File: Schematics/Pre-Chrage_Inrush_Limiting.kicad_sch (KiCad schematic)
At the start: 6 parts, among them J7 464379202, J8 464369202, Q1 STB10NK60ZT4

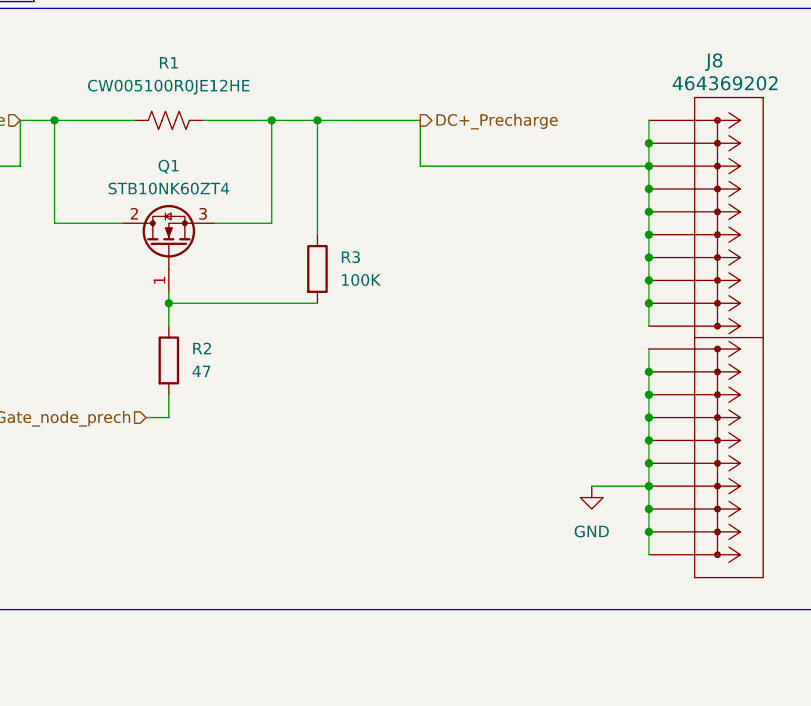
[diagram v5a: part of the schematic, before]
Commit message: [Milestone Compelted Controller and USB]
- Added Test Points
- Completed USB circuit to Controller
- Wired up Controller
- Added Connectors to Power Subsheet and 12pin from cotnroller to Full
  Bridge
- Added 3d models for USB compoents
- General fixes to subsheets
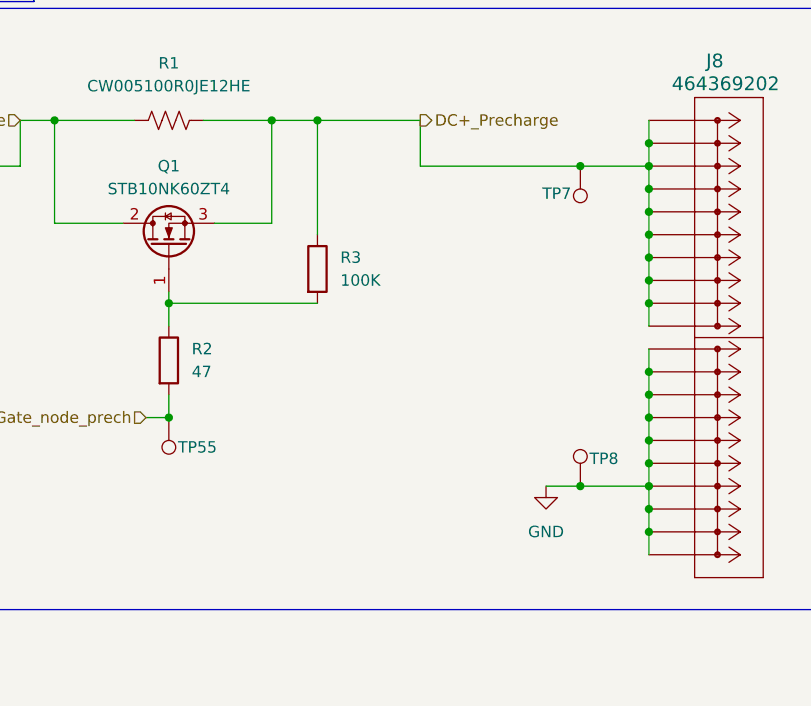
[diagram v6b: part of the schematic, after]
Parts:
- added TP55, TP7: 5277, SiC_Inverter:5277, symbol SiC_Inverter:5277
- added TP8: 5281, SiC_Inverter:5281, symbol SiC_Inverter:5281
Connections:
- net DC+_Precharge: now also TP7.1
- net GND: now also TP8.1
- net Gate_node_prech: now also TP55.1

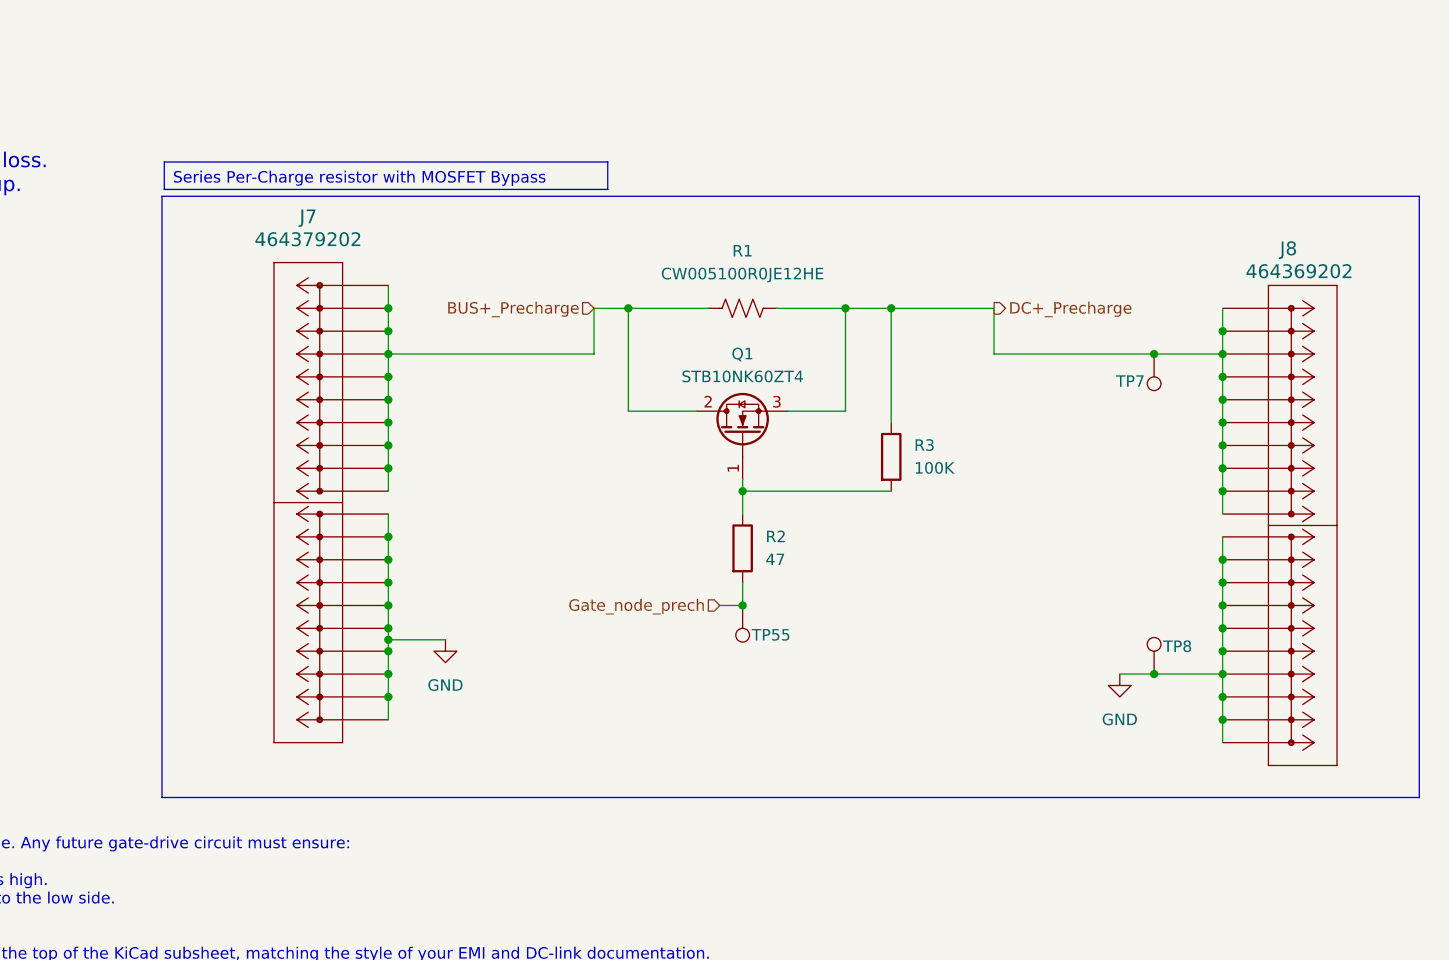
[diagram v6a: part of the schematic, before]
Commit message: [WIP Input Protection Circuit to Controller]
- Added Gate node input protection pin to controller
- Added optocoupler to input protection circuit
- Added 3d model for PC817.....
- Updated PCB to test out PCB modularity
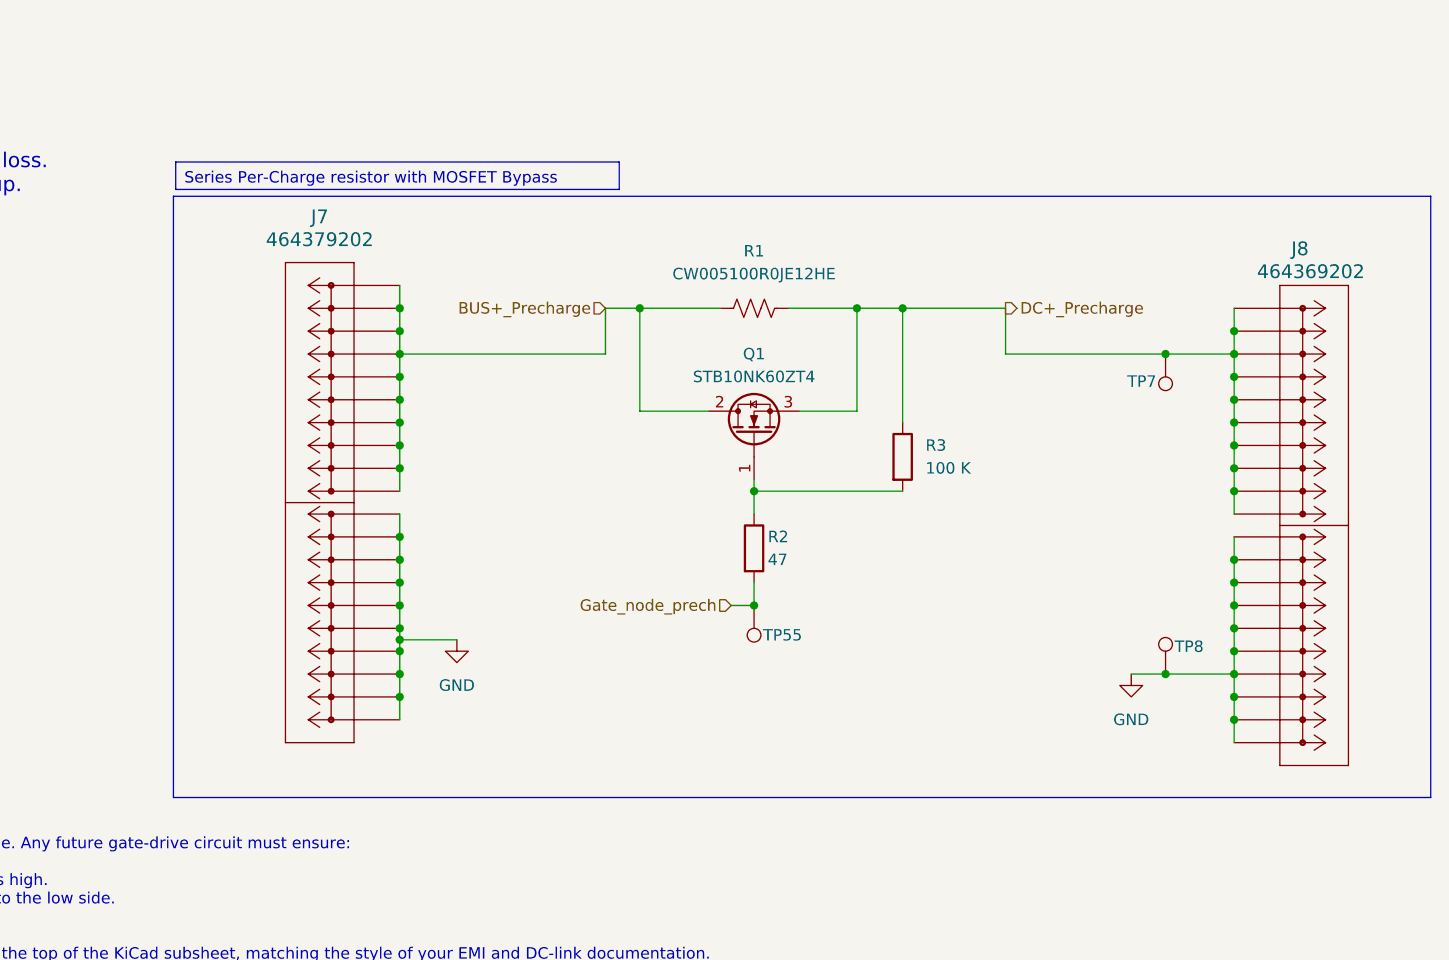
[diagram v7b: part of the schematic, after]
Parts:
- R2: symbol Device:R -> SiC_Inverter:RT1206FRE0747RL
- R3: value 100K -> 100 K; symbol Device:R -> SiC_Inverter:RT1206BRD07100KL
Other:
- moved on the sheet: J7, J8, Q1, R1, R2, R3, TP55, TP7, TP8

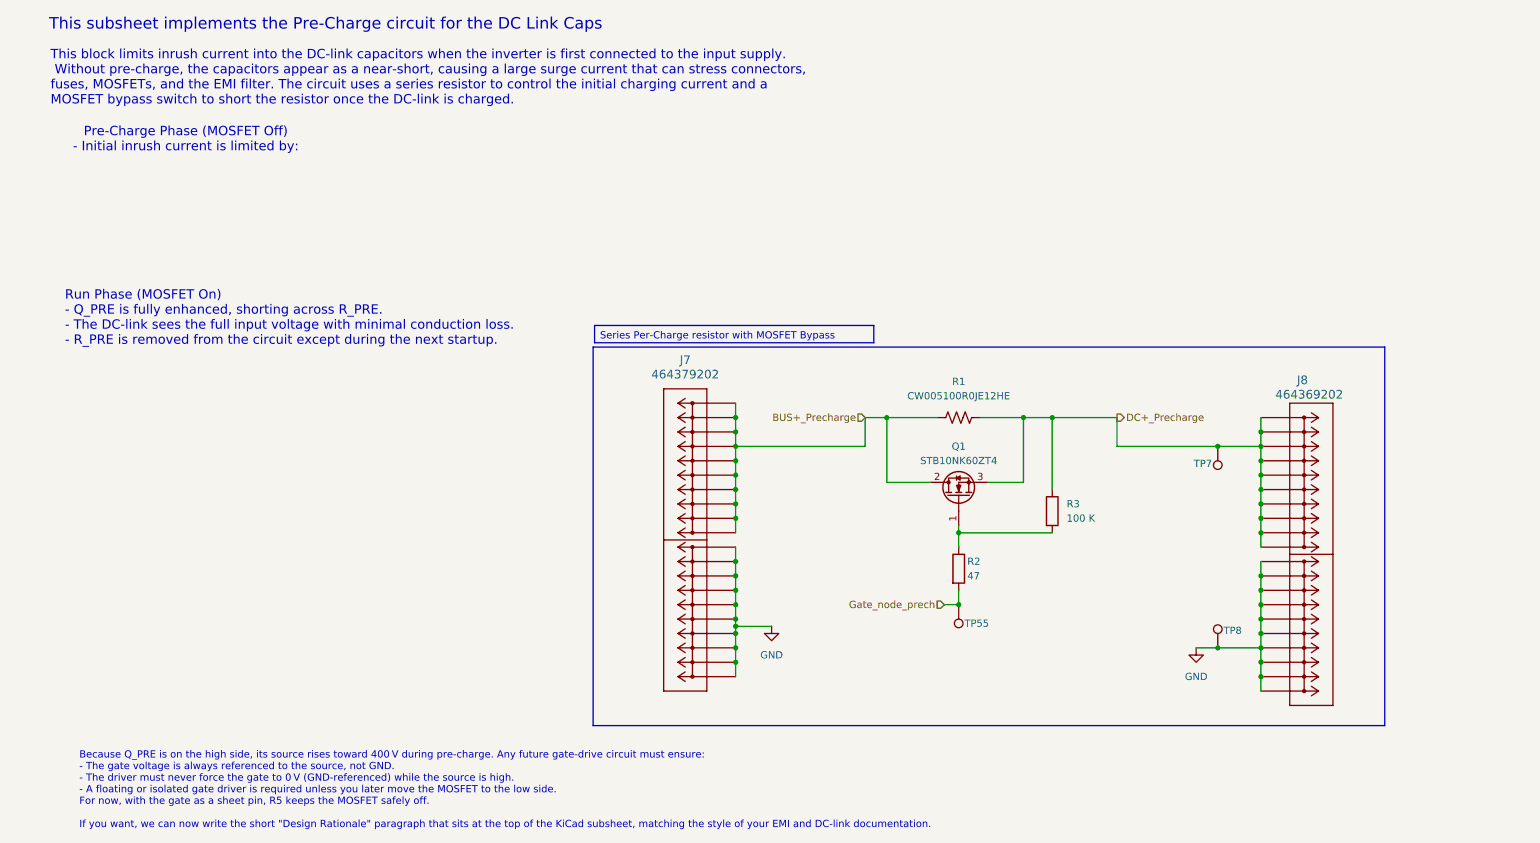
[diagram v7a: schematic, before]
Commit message: Added Precharge Gate Driver to controller and per charge sub circuit
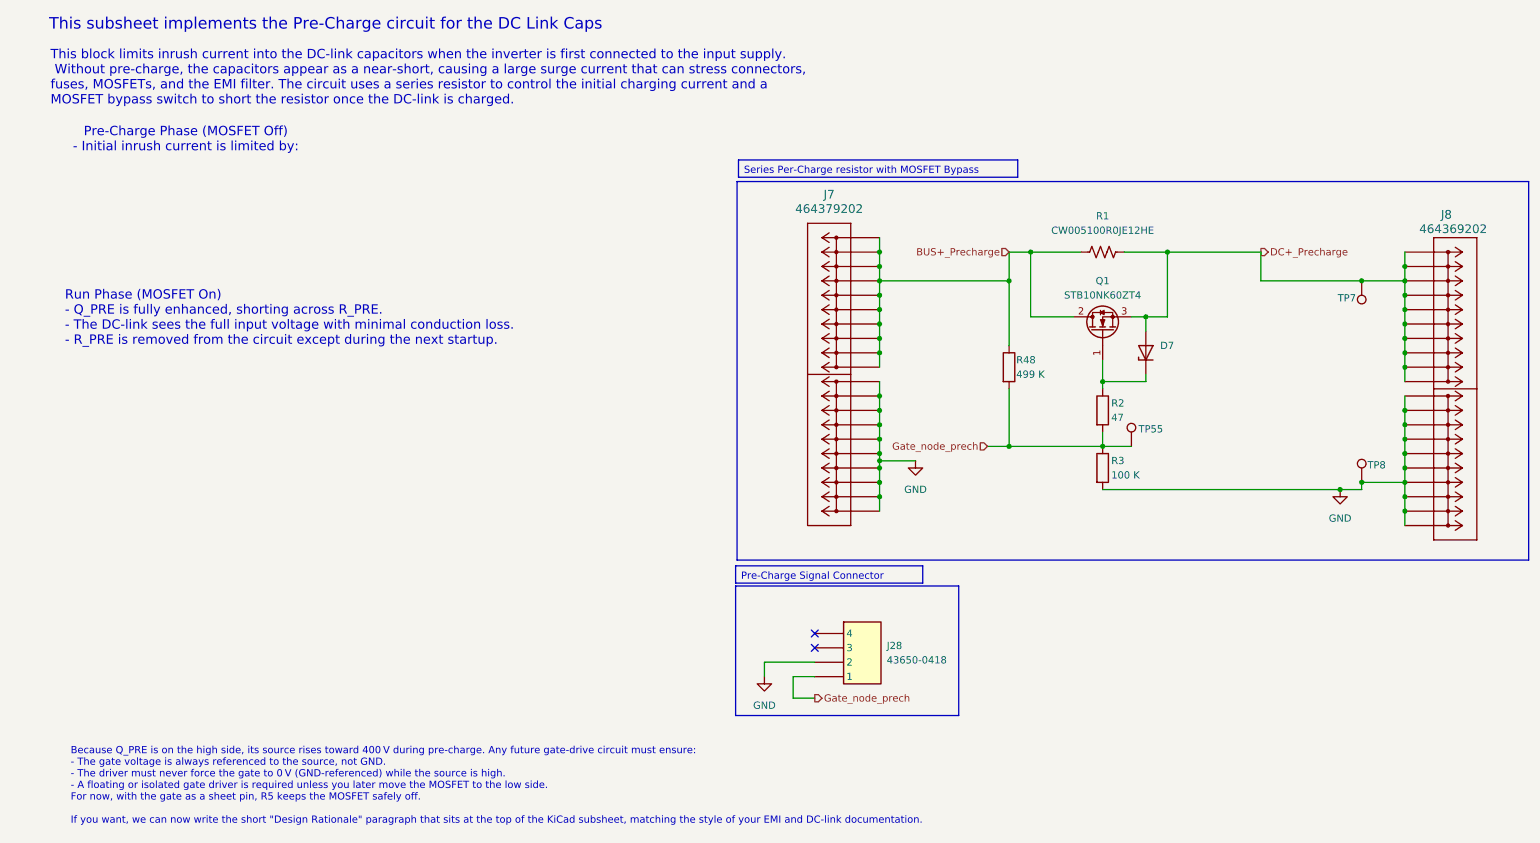
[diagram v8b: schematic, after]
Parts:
- added D7: BZX84C15-7-F, Package_TO_SOT_SMD:SOT-23-3, symbol SiC_Inverter:BZX84C15-7-F
- added J28: 43650-0418, SiC_Inverter:436500418, symbol SiC_Inverter:43650-0418
- added R48: 499 K, Resistor_SMD:R_1206_3216Metric_Pad1.30x1.75mm_HandSolder, symbol SiC_Inverter:RP1206BRD07499KL
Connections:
- net BUS+_Precharge: now also R48.1
- net DC+_Precharge: now also D7.2 (A); no longer R3.1
- net GND: now also R3.2, J28.2
- net Gate_node_prech: now also R3.1, J28.1, R48.2
- net at Q1.1 (G), R2.1: now also D7.1 (K); no longer R3.2
- no-connect marks 0 -> 2
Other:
- moved on the sheet: J7, J8, Q1, R1, R2, R3, TP55, TP7, TP8
